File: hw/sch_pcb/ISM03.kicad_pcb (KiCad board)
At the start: 2 copper layers, 60.5 x 40.1 mm, 98 parts, among them J1 JUMP_3X2, J10 HEADER_2x01_PARALLEL, J11 HEADER_2x01_PARALLEL, J12 HEADER_2x01_PARALLEL, J13 HEADER_2x01_PARALLEL, J14 HEADER_2x01_PARALLEL, J15 HEADER_2x01_PARALLEL, J16 HEADER_2x01_PARALLEL, J17 HEADER_2x01_PARALLEL, J18 HEADER_2x01_PARALLEL, J19 HEADER_2x01_PARALLEL, J2 SMA, J20 HEADER_2x01_PARALLEL, J21 HEADER_2x01_PARALLEL, J22 HEADER_2x01_PARALLEL, J23 HEADER_2x01_PARALLEL, J24 HEADER_1x02, J25 HEADER_1x02, J26 HEADER_2x01_PARALLEL, J3 SMA, J4 JUMP_3X2, J6 HEADER_2x01_PARALLEL, J7 HEADER_2x01_PARALLEL, J8 HEADER_2x01_PARALLEL, J9 HEADER_2x01_PARALLEL, M1 HOLE, M2 HOLE, M3 HOLE, M4 HOLE, Q1 BC817, Q2 BC817, U1 LM1117, U2 Si1060-A-GM, Y1 ABS07-120-32.768KHZ, Y2 ABM3B-30.000MHZ-10-1-U-T

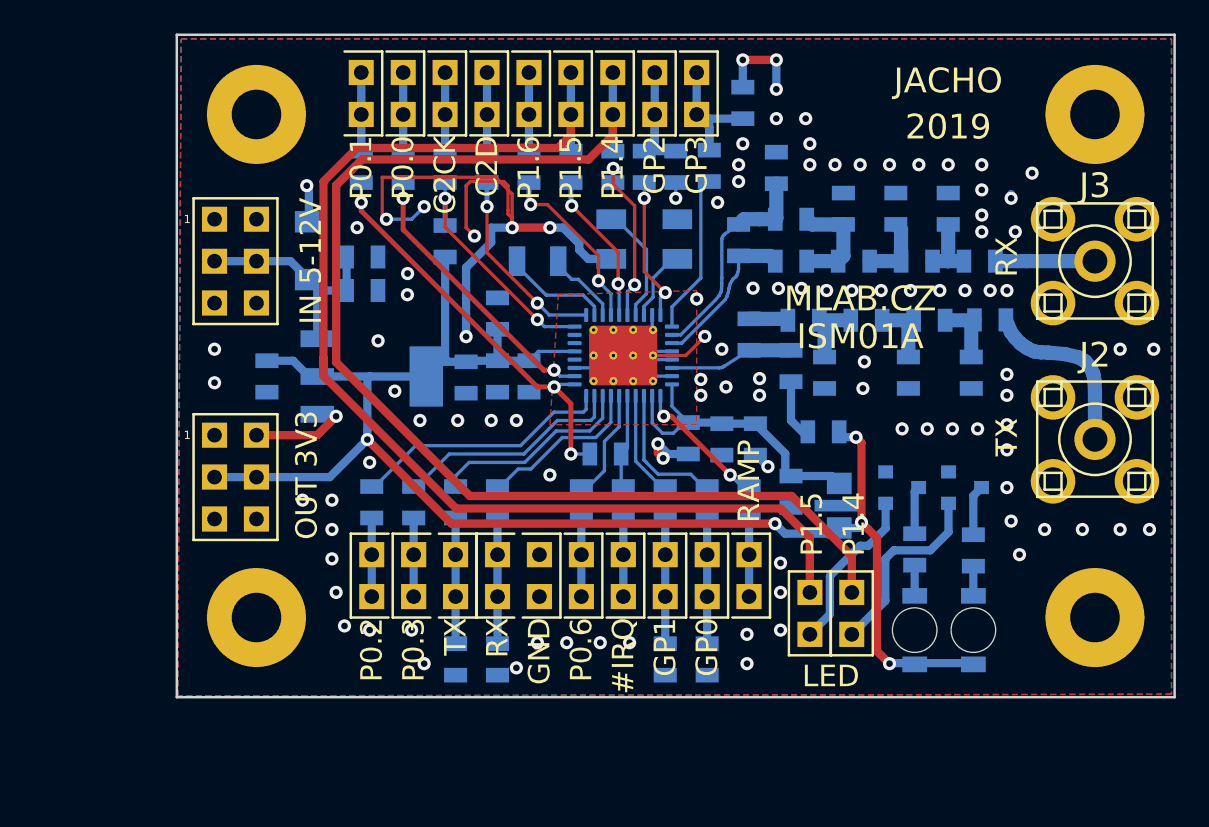
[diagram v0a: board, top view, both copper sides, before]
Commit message: Symplified transceiver WiP.
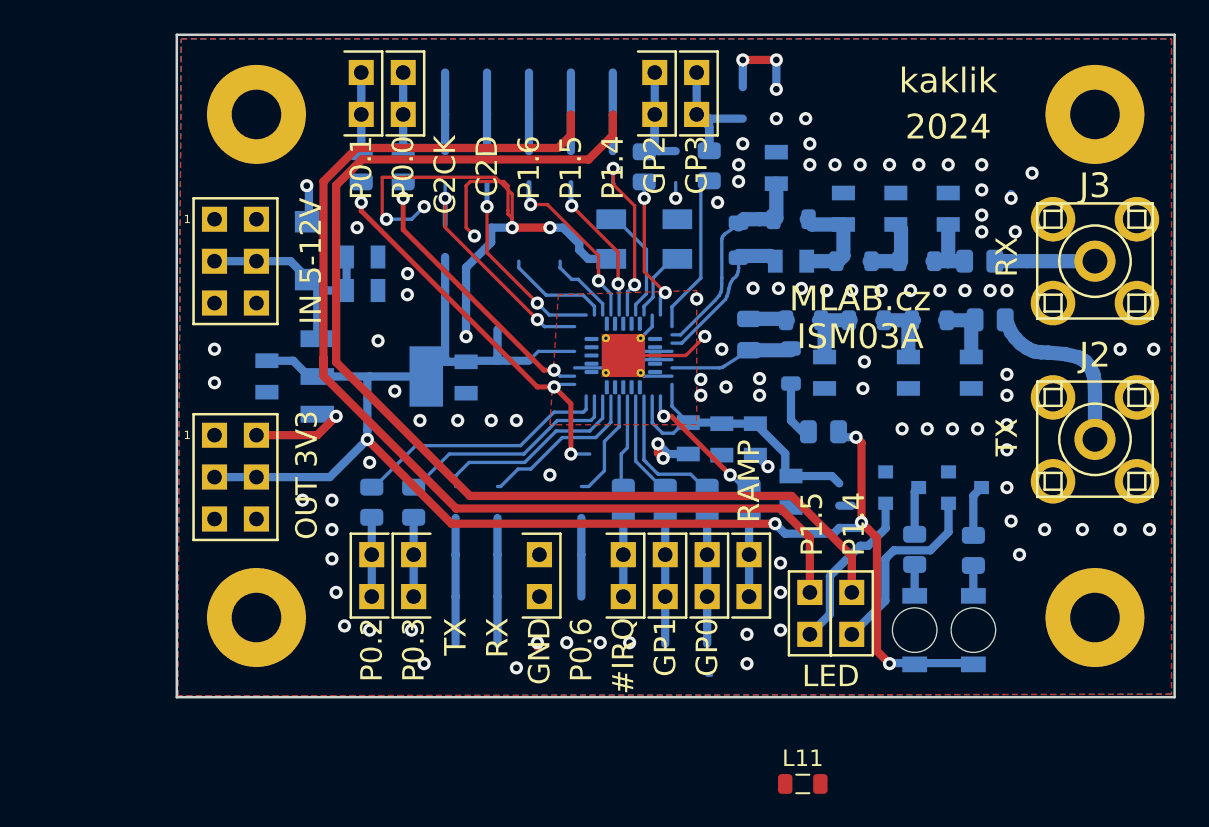
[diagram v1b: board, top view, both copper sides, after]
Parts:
- removed C14, C22, C23, C25, C26, C27, C28: 10nF, Mlab_R:SMD-0805
- removed C16: 100nF, Mlab_R:SMD-0805
- removed C18: 10uF, Mlab_R:SMD-0805
- removed C21: NFM21PC105, Mlab_L:FIR1
- removed J10, J11, J12, J18, J6, J7, J8, J9: HEADER_2x01_PARALLEL, Mlab_Pin_Headers:Straight_2x01
- removed R14, R2, R3, R4, R5, R6, R7, R8: 33R, Mlab_R:SMD-0805
- removed R20: 1k, Mlab_R:SMD-0805
- removed R21: 0R, Mlab_R:SMD-0805
- removed Y1: ABS07-120-32.768KHZ, Mlab_XTAL:ABS07
- added L11: 74279204, Inductor_SMD:L_0805_2012Metric, F.Cu at (160.8, 127.6)
- C11: footprint Mlab_R:SMD-0805 -> Capacitor_SMD:C_0805_2012Metric
- J2, J3: value SMA -> MCX
- L1, L2, R1, R10, R11, R12, R13, R15, R16, R17, R18, R19, R22, R23, R9: footprint Mlab_R:SMD-0805 -> Resistor_SMD:R_0805_2012Metric
- L10, L3, L4, L5, L6, L7, L8, L9: footprint Mlab_R:SMD-0805 -> Inductor_SMD:L_0805_2012Metric
- U1: value LM1117 -> LM1117-3V3
- U2: value Si1060-A-GM -> Si4463; footprint Package_DFN_QFN:QFN-36-1EP_5x6mm_P0.5mm_EP3.6x4.1mm_ThermalVias -> Package_DFN_QFN:QFN-20-1EP_4x4mm_P0.5mm_EP2.6x2.6mm_ThermalVias
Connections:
- net /#IRQ renamed /nIRQ
- net /P0.0 renamed /nSEL
- net /P0.1 renamed /SDO
- net /P0.2 renamed /SDI
- net /P0.3 renamed /SCLK
- C11 pad 1: Net-(C11-Pad1) -> Net-(U2-TX)
- C12 pad 1: Net-(C12-Pad1) -> Net-(U2-RXp)
- C13 pad 1: Net-(C13-Pad1) -> Net-(U2-RXn)
- C3 pad 1: +3V3 -> +3.3V
- C5 pad 1: +3V3 -> +3.3V
- D2 pad 2: +3V3 -> +3.3V
- D3 pad 2: +3V3 -> +3.3V
- J24 pad 2: /P1.4 -> /GPIO2
- J25 pad 2: /P1.5 -> /GPIO3
- J4 pad 3: +3V3 -> +3.3V
- J4 pad 4: +3V3 -> +3.3V
- L10 pad 1: Net-(C13-Pad1) -> Net-(U2-RXn)
- L10 pad 2: Net-(C12-Pad1) -> Net-(U2-RXp)
- L8 pad 2: Net-(C11-Pad1) -> Net-(U2-TX)
- L9 pad 2: Net-(C13-Pad1) -> Net-(U2-RXn)
- R1 pad 1: +3V3 -> +3.3V
- R10 pad 2: Net-(R10-Pad2) -> Net-(U2-SDI)
- R12 pad 2: Net-(R12-Pad2) -> Net-(U2-~{SEL})
- R13 pad 2: Net-(R13-Pad2) -> Net-(U2-TXRAMP)
- R15 pad 2: /#IRQ_1 -> Net-(U2-~{IRQ})
- R16 pad 2: Net-(R16-Pad2) -> Net-(U2-GPIO0)
- R17 pad 2: Net-(R17-Pad2) -> Net-(U2-GPIO1)
- R18 pad 2: Net-(R18-Pad2) -> Net-(U2-GPIO2)
- R19 pad 2: Net-(R19-Pad2) -> Net-(U2-GPIO3)
- R9 pad 2: Net-(R9-Pad2) -> Net-(U2-SCLK)
- U1 pad 2: +3V3 -> +3.3V
- U1 pad 4: +3V3 -> +3.3V
- U2 pad 1: Net-(R2-Pad2) -> unconnected-(U2-SDN-Pad1)
- U2 pad 10: Net-(R18-Pad2) -> Net-(U2-GPIO1)
- U2 pad 11: Net-(R19-Pad2) -> Net-(U2-~{IRQ})
- U2 pad 12: Net-(C13-Pad1) -> Net-(U2-SCLK)
- U2 pad 13: Net-(C12-Pad1) -> /P0.1_1
- U2 pad 14: GND -> Net-(U2-SDI)
- U2 pad 15: GND -> Net-(U2-~{SEL})
- U2 pad 16: Net-(C11-Pad1) -> Net-(U2-XOUT)
- U2 pad 17: GND -> Net-(U2-XIN)
- U2 pad 18: Net-(C15-Pad1) -> GND
- U2 pad 19: Net-(R13-Pad2) -> Net-(U2-GPIO2)
- U2 pad 2: Net-(U2-Pad2) -> Net-(U2-RXp)
- U2 pad 20: Net-(C15-Pad1) -> Net-(U2-GPIO3)
- U2 pad 21: Net-(R16-Pad2) -> GND
- U2 pad 3: Net-(U2-Pad3) -> Net-(U2-RXn)
- U2 pad 4: Net-(R3-Pad2) -> Net-(U2-TX)
- U2 pad 5: Net-(R4-Pad2) -> unconnected-(U2-NC-Pad5)
- U2 pad 6: Net-(R5-Pad2) -> Net-(C15-Pad1)
- U2 pad 7: Net-(U2-Pad7) -> Net-(U2-TXRAMP)
- U2 pad 8: Net-(U2-Pad8) -> Net-(C15-Pad1)
- U2 pad 9: GND -> Net-(U2-GPIO0)
- Y2 pad 1: Net-(U2-Pad8) -> Net-(U2-XIN)
- Y2 pad 3: Net-(U2-Pad7) -> Net-(U2-XOUT)
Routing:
- net +3V3: track 96.7 -> 0.00 mm, vias 5 -> 0
- net +3.3V: track 0.00 -> 96.7 mm, vias 0 -> 5
- net /P1.4: track 73.1 -> 0.00 mm
- net /P1.5: track 71.3 -> 0.00 mm
- net /GPIO2: track 9.26 -> 77.6 mm
- net /GPIO3: track 9.82 -> 76.3 mm
- net (no net): track 0.00 -> 43.8 mm
- net Net-(U2-~{SEL}): track 0.00 -> 16.9 mm, vias 0 -> 2
- net Net-(R12-Pad2): track 16.9 -> 0.00 mm, vias 2 -> 0
- net Net-(U2-SDI): track 0.00 -> 15.7 mm
- net Net-(R10-Pad2): track 15.7 -> 0.00 mm
- net Net-(U2-SCLK): track 0.00 -> 14.0 mm
- net Net-(R9-Pad2): track 14.0 -> 0.00 mm
- net Net-(U2-RXn): track 0.00 -> 13.5 mm
- net Net-(C13-Pad1): track 13.5 -> 0.00 mm
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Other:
- board text added: "2024"
- board text added: "ISM03A"
- board text added: "MLAB.cz"
- board text added: "kaklik"
- board text removed: "2019"
- board text removed: "ISM01A"
- board text removed: "JACHO"
- board text removed: "MLAB.CZ"

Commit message: Update documentation PCB WiP.
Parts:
- added R2: 1k, Resistor_SMD:R_0805_2012Metric, B.Cu at (158.5, 124.0)
- added R3: 1k, Resistor_SMD:R_0805_2012Metric, B.Cu at (158.5, 127.0)
- C1, C10, C12, C13, C15, C17, C19, C2, C20, C3, C4, C5, C6, C7, C8, C9: footprint Mlab_R:SMD-0805 -> Capacitor_SMD:C_0805_2012Metric
- D1: footprint Mlab_D:Diode-MiniMELF_Standard -> Diode_SMD:D_SMA
- L11: moved to B.Cu
- R1: value 0R -> 3R
- moved J19 30.8 mm to (137.1, 87.0), turned to -90 degrees
- moved J14 30.4 mm to (144.8, 86.4), turned to 90 degrees
- moved J13 28.1 mm to (139.7, 87.0), turned to 90 degrees
- moved R15 23.0 mm to (137.1, 91.4), turned to -90 degrees
- moved R10 22.2 mm to (144.8, 90.8), turned to -90 degrees
- moved R9 19.3 mm to (139.7, 91.4), turned to -90 degrees
- moved J16 10.8 mm to (147.3, 85.8)
- moved R12 10.8 mm to (147.3, 90.2)
- moved J15 8.23 mm to (142.2, 85.8)
- moved R11 8.23 mm to (142.2, 90.2)
- moved J26 7.65 mm to (137.2, 115.0)
- moved L11 7.19 mm to (168.0, 127.6), turned to 180 degrees
- moved R19 2.69 mm to (152.4, 90.2)
- moved Y2 2.07 mm to (149.3, 95.6)
- moved J22 1.93 mm to (149.9, 85.8)
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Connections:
- C12 pad 1: Net-(U2-RXp) -> Net-(U2-RXn)
- C13 pad 1: Net-(U2-RXn) -> Net-(U2-RXp)
- J24 pad 1: Net-(Q1-B) -> Net-(J24-Pad1)
- J25 pad 1: Net-(Q2-B) -> Net-(J25-Pad1)
- L10 pad 1: Net-(U2-RXn) -> Net-(U2-RXp)
- L10 pad 2: Net-(U2-RXp) -> Net-(U2-RXn)
- L9 pad 2: Net-(U2-RXn) -> Net-(U2-RXp)
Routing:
- net GND: track 81.8 -> 2.49 mm, vias 105 -> 100
- net +3.3V: track 96.7 -> 21.9 mm
- net /GPIO3: track 76.3 -> 5.81 mm
- net /GPIO2: track 77.6 -> 7.35 mm
- net (no net): track 43.8 -> 0.00 mm
- net /P0.1_1: track 24.8 -> 0.00 mm, vias 3 -> 0
- net Net-(U2-~{SEL}): track 16.9 -> 0.00 mm, vias 2 -> 0
- net Net-(U2-SDI): track 15.7 -> 0.00 mm
- net /#RST_1: track 14.7 -> 0.00 mm, vias 2 -> 0
- net VCC: track 14.6 -> 0.00 mm
- net Net-(U2-SCLK): track 14.0 -> 0.00 mm
- net Net-(R8-Pad2): track 12.3 -> 0.00 mm
- net Net-(R2-Pad2): track 11.8 -> 0.00 mm, vias 2 -> 0
- net Net-(C15-Pad1): track 17.8 -> 6.68 mm
- net Net-(U2-RXn): track 13.5 -> 2.35 mm
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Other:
- board text removed: "C2CK"
- board text removed: "C2D"
- board text removed: "P0.0"
- board text removed: "P0.1"
- board text removed: "P0.2"
- board text removed: "P0.3"

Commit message: Backup work before switching to KiCADv8
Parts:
- added J5: HEADER_2x01_PARALLEL, Mlab_Pin_Headers:Straight_2x01, F.Cu at (142.7, 89.0)
- added R4: 33R, Resistor_SMD:R_0805_2012Metric, B.Cu at (144.0, 96.7)
- added R5: 10k, Resistor_SMD:R_0805_2012Metric, B.Cu at (144.0, 92.9)
- R2, R3: value 1k -> 10k
- moved J24 42.4 mm to (132.6, 88.5)
- moved R3 39.4 mm to (148.8, 88.8), turned to 0 degrees
- moved M4 38.6 mm to (168.8, 120.2)
- moved R2 38.5 mm to (148.8, 86.8), turned to 0 degrees
- moved C5 37.2 mm to (161.3, 120.0)
- moved J25 35.2 mm to (140.2, 89.0)
- moved D2 32.8 mm to (161.4, 87.0), turned to 180 degrees
- moved R22 30.2 mm to (156.5, 87.0), turned to 180 degrees
- moved M2 29.4 mm to (168.8, 89.8)
- moved Q1 28.5 mm to (152.7, 87.5), turned to 90 degrees
- moved D3 28.4 mm to (161.4, 90.6), turned to 180 degrees
- moved R23 25.4 mm to (156.5, 90.6), turned to 180 degrees
- moved U1 25.1 mm to (153.3, 119.7)
- moved C3 25.1 mm to (159.0, 119.8)
- moved J19 24.1 mm to (130.1, 110.1), turned to 0 degrees
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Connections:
- U2 pad 1: unconnected-(U2-SDN-Pad1) -> Net-(U2-SDN)
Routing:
- net +3.3V: track 21.9 -> 0.00 mm, vias 5 -> 0
- net Net-(Q1-B): track 11.7 -> 0.00 mm
- net /GPIO2: track 7.35 -> 0.00 mm
- net Net-(C15-Pad1): track 6.68 -> 0.00 mm
- net /GPIO3: track 5.81 -> 0.00 mm
- net Net-(J25-Pad1): track 4.03 -> 0.00 mm
- net Net-(Q1-C): track 3.06 -> 0.00 mm
- net Net-(Q2-C): track 2.89 -> 0.00 mm
- net Net-(Q2-B): track 2.01 -> 0.00 mm
- net Net-(D3-K): track 1.94 -> 0.00 mm
- net Net-(D2-K): track 1.87 -> 0.00 mm
- net GND: track 2.49 -> 0.74 mm, vias 100 -> 79
- net Net-(U2-~{IRQ}): vias 1 -> 0
- net /SDO: vias 0 -> 1
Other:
- board size 60.5 x 40.1 mm -> 50.3 x 40.1 mm
